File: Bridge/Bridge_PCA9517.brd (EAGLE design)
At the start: 13 x 17 mm, 15 parts, among them IC1 BMP085, X1 EOC, X12 XCLR, X2 3v3, X3 GND, X4 SCL, X5 SDA, X6 3v3, X7 GND, X8 SCL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

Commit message: Typo correction and more elegance presentation
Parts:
- removed X1: EOC, Conn:S1.27R
- removed X12: XCLR, Conn:S1.27R
- added C2: 100n, RCL:0603
- added R4: 10k, RCL:0603
- IC1: value BMP085 -> PCA9517D; device Sensors:LCC8 -> Other:SOIC8
- X4: value SCL -> SCLA
- X5: value SDA -> SDAA
- X6: value 3v3 -> 5V
- X8: value SCL -> SCLB
- X9: value SDA -> SDAB
- moved R3 8.92 mm to (6.10, 3.94), turned to 180 degrees
- moved R2 8.15 mm to (3.30, 8.26)
- moved R1 4.16 mm to (10.3, 9.78), turned to 90 degrees
- moved C1 2.70 mm to (2.79, 6.10), turned to 0 degrees
- moved IC1 0.74 mm to (6.86, 8.76)
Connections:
- removed net EOC: IC1.2, X1.1
- removed net SCL: IC1.6, R3.1, X4.1, X8.1
- removed net SDA: IC1.7, R2.1, X5.1, X9.1
- removed net XCLR: IC1.8, R1.2, X12.1
- new net N$3: C2.2, IC1.8, R1.2, R4.2, X6.1
- new net SCLA: IC1.2, R3.1, X4.1
- new net SCLB: IC1.7, R1.1, X8.1
- new net SDAA: IC1.3, R2.1, X5.1
- new net SDAB: IC1.6, R4.1, X9.1
- net +3V3: now also IC1.1; no longer IC1.3, IC1.4, R1.1, X6.1
- net GND: now also C2.1, IC1.4; no longer IC1.1
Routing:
- net SDA: track 23.3 -> 0.00 mm
- net SCL: track 23.0 -> 0.00 mm
- net +3V3: track 29.8 -> 9.68 mm
- net N$3: track 0.00 -> 17.6 mm
- net SDAA: track 0.00 -> 11.4 mm
- net SCLB: track 0.00 -> 9.77 mm
- net SDAB: track 0.00 -> 6.16 mm
- net SCLA: track 0.00 -> 4.64 mm
- net XCLR: track 4.44 -> 0.00 mm
- net EOC: track 1.78 -> 0.00 mm

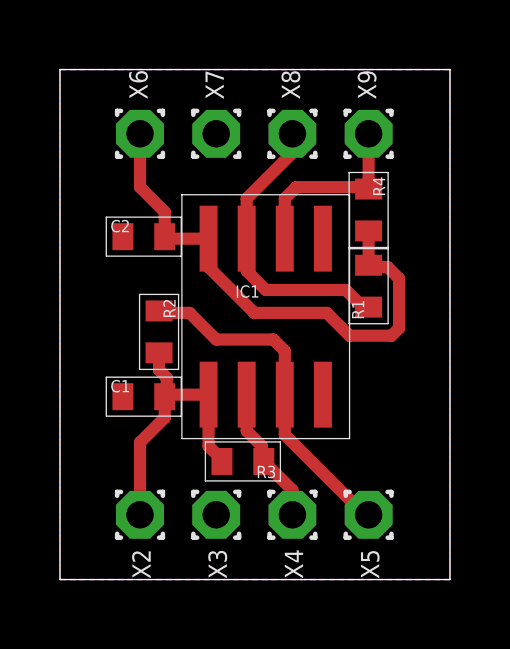
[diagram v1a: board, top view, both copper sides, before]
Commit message: I2C to I2C bridge/Level translator
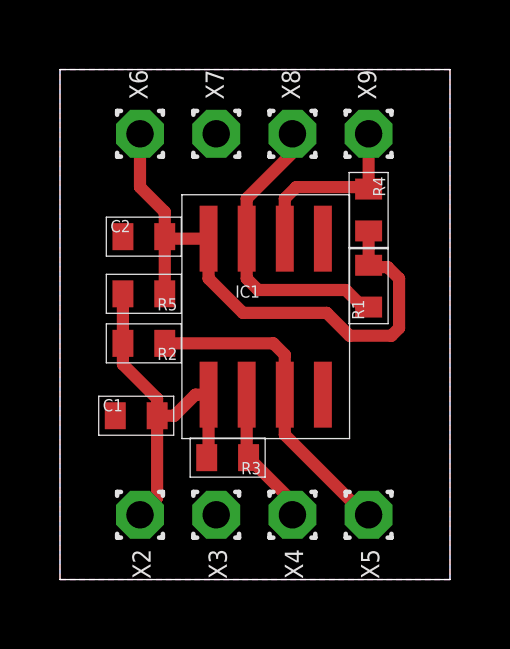
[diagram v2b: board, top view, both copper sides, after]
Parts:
- added R5: n.b., RCL:0603
- moved C1 0.68 mm to (2.54, 5.46)
- moved R2 0.64 mm to (2.79, 7.87), turned to 180 degrees
- moved R3 0.52 mm to (5.59, 4.06)
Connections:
- net +3V3: now also R5.2
- net N$3: now also R5.1
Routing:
- net +3V3: track 9.68 -> 12.2 mm
- net N$3: track 17.6 -> 19.7 mm
- net SDAA: track 11.4 -> 10.7 mm
